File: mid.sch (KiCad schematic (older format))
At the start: 26 parts, among them P1 POLOLU_MICROSD1, P2 ADAFRUIT_MICROSD1, P3 EBAY_MICROSD1, P4 POLOLU_MICROSD2, P5 ADAFRUIT_MICROSD2, P6 EBAY_MICROSD2, P7 SPI, P8 RC2014_STANDARD_DEV_39, SW1 SW_DIP_x04, U1 TP3465-PLCC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

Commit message: add PCB
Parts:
- removed P7: SPI, symbol CONN_01X08
- added P7: SPI, Connector_PinHeader_2.54mm:PinHeader_1x09_P2.54mm_Vertical, symbol CONN_01X09
- C1, C2, C3: footprint (none) -> Capacitor_THT:C_Rect_L4.6mm_W2.0mm_P2.50mm_MKS02_FKP02
- C4: footprint (none) -> Capacitor_THT:CP_Radial_D5.0mm_P2.00mm
- JP1: footprint (none) -> Connector_PinHeader_2.54mm:PinHeader_1x02_P2.54mm_Vertical
- JP2, JP3: footprint (none) -> Connector_PinHeader_2.54mm:PinHeader_1x03_P2.54mm_Vertical
- P1, P4: footprint (none) -> Connector_PinHeader_2.54mm:PinHeader_1x09_P2.54mm_Vertical
- P2, P5: footprint (none) -> Connector_PinHeader_2.54mm:PinHeader_1x08_P2.54mm_Vertical
- P3, P6: footprint (none) -> Connector_PinHeader_2.54mm:PinHeader_1x06_P2.54mm_Vertical
- P8: footprint (none) -> Connector_PinHeader_2.54mm:PinHeader_1x39_P2.54mm_Vertical
- R1, R2, R3, R4, R5, R6, R7, R8: footprint (none) -> Resistor_THT:R_Axial_DIN0207_L6.3mm_D2.5mm_P7.62mm_Horizontal
- SW1: footprint (none) -> Button_Switch_THT:SW_DIP_SPSTx04_Piano_CTS_Series194-4MSTN_W7.62mm_P2.54mm
- U1: footprint (none) -> Package_LCC:PLCC-28_THT-Socket
- U2: footprint (none) -> Package_DIP:DIP-20_W7.62mm_Socket
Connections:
- net GND: now also P7.1 (P1)
- net MISO: now also P7.7 (P7)
- net MOSI: now also P7.8 (P8)
- net SCLK: now also P7.9 (P9)
- net VCC: now also P7.2 (P2)
- net ~SDCD1: now also P7.4 (P4)
- net ~SDCD2: now also P7.3 (P3)
- net ~SDCS1: now also P7.6 (P6)
- net ~SDCS2: now also P7.5 (P5)
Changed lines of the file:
@@
 LIBS:Switch
 LIBS:my_components
+LIBS:mid-cache
 EELAYER 25 0
 EELAYER END
@@
 Sheet 1 1
 Title "RC2014 MID"
-Date "2020-04-04"
+Date "2020-04-06"
 Rev ""
 Comp ""
@@
 F 0 "P8" H 2250 5950 50  0000 C CNN
 F 1 "RC2014_STANDARD_DEV_39" V 2000 3950 50  0000 C CNN
-F 2 "" H 2250 3950 50  0000 C CNN
+F 2 "Connector_PinHeader_2.54mm:PinHeader_1x39_P2.54mm_Vertical" H 2250 3950 50  0001 C CNN
 F 3 "" H 2250 3950 50  0000 C CNN
 	1    2250 3950
@@
 F 0 "U2" H 3550 4000 60  0000 L CNN
 F 1 "74HCT688" H 3550 2700 60  0000 L CNN
-F 2 "" H 3850 3350 60  0001 C CNN
+F 2 "Package_DIP:DIP-20_W7.62mm_Socket" H 3850 3350 60  0001 C CNN
 F 3 "" H 3850 3350 60  0001 C CNN
 	1    3850 3350
@@
 F 0 "SW1" H 5200 3900 50  0000 C CNN
 F 1 "SW_DIP_x04" H 5200 3300 50  0000 C CNN
-F 2 "" H 5200 3550 50  0001 C CNN
+F 2 "Button_Switch_THT:SW_DIP_SPSTx04_Piano_CTS_Series194-4MSTN_W7.62mm_P2.54mm" H 5200 3550 50  0001 C CNN
 F 3 "" H 5200 3550 50  0001 C CNN
 	1    5200 3550
@@
 F 0 "P2" H 7450 4450 50  0000 C CNN
 F 1 "ADAFRUIT_MICROSD1" V 7550 4000 50  0000 C CNN
-F 2 "" H 7450 4000 50  0000 C CNN
+F 2 "Connector_PinHeader_2.54mm:PinHeader_1x08_P2.54mm_Vertical" H 7450 4000 50  0001 C CNN
 F 3 "" H 7450 4000 50  0000 C CNN
 	1    7450 4000
@@
 F 0 "U1" H 4850 6700 60  0000 L CNN
 F 1 "TP3465-PLCC" H 4850 4500 60  0000 L CNN
-F 2 "" H 5150 5250 60  0001 C CNN
+F 2 "Package_LCC:PLCC-28_THT-Socket" H 5150 5250 60  0001 C CNN
 F 3 "" H 5150 5250 60  0001 C CNN
 	1    5150 5600
@@
 F 0 "R2" V 5050 2700 50  0000 L CNN
 F 1 "10K" V 5000 2600 50  0000 C CNN
-F 2 "" V 4930 2600 50  0000 C CNN
+F 2 "Resistor_THT:R_Axial_DIN0207_L6.3mm_D2.5mm_P7.62mm_Horizontal" V 4930 2600 50  0001 C CNN
 F 3 "" H 5000 2600 50  0000 C CNN
 	1    5000 2600
@@
 F 0 "R1" V 4950 2700 50  0000 L CNN
 F 1 "10K" V 4900 2600 50  0000 C CNN
-F 2 "" V 4830 2600 50  0000 C CNN
+F 2 "Resistor_THT:R_Axial_DIN0207_L6.3mm_D2.5mm_P7.62mm_Horizontal" V 4830 2600 50  0001 C CNN
 F 3 "" H 4900 2600 50  0000 C CNN
 	1    4900 2600
@@
 F 0 "R3" V 5150 2700 50  0000 L CNN
 F 1 "10K" V 5100 2600 50  0000 C CNN
-F 2 "" V 5030 2600 50  0000 C CNN
+F 2 "Resistor_THT:R_Axial_DIN0207_L6.3mm_D2.5mm_P7.62mm_Horizontal" V 5030 2600 50  0001 C CNN
 F 3 "" H 5100 2600 50  0000 C CNN
 	1    5100 2600
@@
 F 0 "R4" V 5250 2700 50  0000 L CNN
 F 1 "10K" V 5200 2600 50  0000 C CNN
-F 2 "" V 5130 2600 50  0000 C CNN
+F 2 "Resistor_THT:R_Axial_DIN0207_L6.3mm_D2.5mm_P7.62mm_Horizontal" V 5130 2600 50  0001 C CNN
 F 3 "" H 5200 2600 50  0000 C CNN
 	1    5200 2600
@@
 F 0 "R5" V 5350 2700 50  0000 L CNN
 F 1 "10K" V 5300 2600 50  0000 C CNN
-F 2 "" V 5230 2600 50  0000 C CNN
+F 2 "Resistor_THT:R_Axial_DIN0207_L6.3mm_D2.5mm_P7.62mm_Horizontal" V 5230 2600 50  0001 C CNN
 F 3 "" H 5300 2600 50  0000 C CNN
 	1    5300 2600
@@
 F 0 "R7" V 6550 1900 50  0000 C CNN
 F 1 "10K" V 6450 1900 50  0000 C CNN
-F 2 "" V 6380 1900 50  0000 C CNN
+F 2 "Resistor_THT:R_Axial_DIN0207_L6.3mm_D2.5mm_P7.62mm_Horizontal" V 6380 1900 50  0001 C CNN
 F 3 "" H 6450 1900 50  0000 C CNN
 	1    6450 1900
@@
 F 0 "JP2" H 6500 1450 50  0000 L CNN
 F 1 "SDCD1_PULL" H 6450 1650 50  0000 C BNN
-F 2 "" H 6450 1550 50  0000 C CNN
+F 2 "Connector_PinHeader_2.54mm:PinHeader_1x03_P2.54mm_Vertical" H 6450 1550 50  0001 C CNN
 F 3 "" H 6450 1550 50  0000 C CNN
 	1    6450 1550
@@
 F 0 "P3" H 7450 6050 50  0000 C CNN
 F 1 "EBAY_MICROSD1" V 7550 5700 50  0000 C CNN
-F 2 "" H 7450 5700 50  0000 C CNN
+F 2 "Connector_PinHeader_2.54mm:PinHeader_1x06_P2.54mm_Vertical" H 7450 5700 50  0001 C CNN
 F 3 "" H 7450 5700 50  0000 C CNN
 	1    7450 5700
@@
 F 0 "P4" H 9050 3450 50  0000 C CNN
 F 1 "POLOLU_MICROSD2" V 9150 2950 50  0000 C CNN
-F 2 "" H 9050 2950 50  0000 C CNN
+F 2 "Connector_PinHeader_2.54mm:PinHeader_1x09_P2.54mm_Vertical" H 9050 2950 50  0001 C CNN
 F 3 "" H 9050 2950 50  0000 C CNN
 	1    9050 2950
@@
 F 0 "P1" H 7450 3450 50  0000 C CNN
 F 1 "POLOLU_MICROSD1" V 7550 2950 50  0000 C CNN
-F 2 "" H 7450 2950 50  0000 C CNN
+F 2 "Connector_PinHeader_2.54mm:PinHeader_1x09_P2.54mm_Vertical" H 7450 2950 50  0001 C CNN
 F 3 "" H 7450 2950 50  0000 C CNN
 	1    7450 2950
@@
 F 0 "P5" H 9050 4450 50  0000 C CNN
 F 1 "ADAFRUIT_MICROSD2" V 9150 4000 50  0000 C CNN
-F 2 "" H 9050 4000 50  0000 C CNN
+F 2 "Connector_PinHeader_2.54mm:PinHeader_1x08_P2.54mm_Vertical" H 9050 4000 50  0001 C CNN
 F 3 "" H 9050 4000 50  0000 C CNN
 	1    9050 4000
@@
 F 0 "P6" H 9050 6050 50  0000 C CNN
 F 1 "EBAY_MICROSD2" V 9150 5700 50  0000 C CNN
-F 2 "" H 9050 5700 50  0000 C CNN
+F 2 "Connector_PinHeader_2.54mm:PinHeader_1x06_P2.54mm_Vertical" H 9050 5700 50  0001 C CNN
 F 3 "" H 9050 5700 50  0000 C CNN
 	1    9050 5700
@@
 F 0 "JP1" H 6100 2430 50  0000 C CNN
 F 1 "MISO_PULLUP" H 6110 2290 50  0000 C CNN
-F 2 "" H 6100 2350 50  0000 C CNN
+F 2 "Connector_PinHeader_2.54mm:PinHeader_1x02_P2.54mm_Vertical" H 6100 2350 50  0001 C CNN
 F 3 "" H 6100 2350 50  0000 C CNN
 	1    6100 2350
@@
 F 0 "R6" V 6200 1900 50  0000 C CNN
 F 1 "10K" V 6100 1900 50  0000 C CNN
-F 2 "" V 6030 1900 50  0000 C CNN
+F 2 "Resistor_THT:R_Axial_DIN0207_L6.3mm_D2.5mm_P7.62mm_Horizontal" V 6030 1900 50  0001 C CNN
 F 3 "" H 6100 1900 50  0000 C CNN
 	1    6100 1900
@@
 F 0 "R8" V 8150 1950 50  0000 C CNN
 F 1 "10K" V 8050 1950 50  0000 C CNN
-F 2 "" V 7980 1950 50  0000 C CNN
+F 2 "Resistor_THT:R_Axial_DIN0207_L6.3mm_D2.5mm_P7.62mm_Horizontal" V 7980 1950 50  0001 C CNN
 F 3 "" H 8050 1950 50  0000 C CNN
 	1    8050 1950
@@
 F 0 "JP3" H 8100 1450 50  0000 L CNN
 F 1 "SDCD2_PULL" H 8050 1650 50  0000 C BNN
-F 2 "" H 8050 1550 50  0000 C CNN
+F 2 "Connector_PinHeader_2.54mm:PinHeader_1x03_P2.54mm_Vertical" H 8050 1550 50  0001 C CNN
 F 3 "" H 8050 1550 50  0000 C CNN
 	1    8050 1550
@@
 F 0 "C4" H 3310 7520 50  0000 L CNN
 F 1 "10µF" H 3310 7370 50  0000 L CNN
-F 2 "" H 3300 7450 50  0000 C CNN
+F 2 "Capacitor_THT:CP_Radial_D5.0mm_P2.00mm" H 3300 7450 50  0001 C CNN
 F 3 "" H 3300 7450 50  0000 C CNN
 	1    3300 7450
@@
 F 0 "C2" H 2510 7520 50  0000 L CNN
 F 1 "100nF" H 2510 7370 50  0000 L CNN
-F 2 "" H 2500 7450 50  0000 C CNN
+F 2 "Capacitor_THT:C_Rect_L4.6mm_W2.0mm_P2.50mm_MKS02_FKP02" H 2500 7450 50  0001 C CNN
 F 3 "" H 2500 7450 50  0000 C CNN
 	1    2500 7450
@@
 F 0 "C3" H 2910 7520 50  0000 L CNN
 F 1 "100nF" H 2910 7370 50  0000 L CNN
-F 2 "" H 2900 7450 50  0000 C CNN
+F 2 "Capacitor_THT:C_Rect_L4.6mm_W2.0mm_P2.50mm_MKS02_FKP02" H 2900 7450 50  0001 C CNN
 F 3 "" H 2900 7450 50  0000 C CNN
 	1    2900 7450
@@
 F 0 "C1" H 2110 7520 50  0000 L CNN
 F 1 "100nF" H 2110 7370 50  0000 L CNN
-F 2 "" H 2100 7450 50  0000 C CNN
+F 2 "Capacitor_THT:C_Rect_L4.6mm_W2.0mm_P2.50mm_MKS02_FKP02" H 2100 7450 50  0001 C CNN
 F 3 "" H 2100 7450 50  0000 C CNN
 	1    2100 7450
@@
 	3300 7550 3300 7600
 Connection ~ 3300 7600
-$Comp
-L CONN_01X08 P7
-U 1 1 5E8A7DE2
-P 10250 5000
-F 0 "P7" H 10250 5450 50  0000 C CNN
-F 1 "SPI" V 10350 5000 50  0000 C CNN
-F 2 "" H 10250 5000 50  0000 C CNN
-F 3 "" H 10250 5000 50  0000 C CNN
-	1    10250 5000
-	1    0    0    1
-$EndComp
 Connection ~ 6450 5150
 Connection ~ 8050 5250
@@
 L GND #PWR014
 U 1 1 5E8A8639
-P 9450 6050
-F 0 "#PWR014" H 9450 5800 50  0001 C CNN
-F 1 "GND" H 9450 5900 50  0000 C CNN
-F 2 "" H 9450 6050 50  0000 C CNN
-F 3 "" H 9450 6050 50  0000 C CNN
-	1    9450 6050
-	1    0    0    -1
-$EndComp
-Wire Wire Line
-	10050 5350 9450 5350
-Wire Wire Line
-	9450 5350 9450 6050
+P 9950 5550
+F 0 "#PWR014" H 9950 5300 50  0001 C CNN
+F 1 "GND" H 9950 5400 50  0000 C CNN
+F 2 "" H 9950 5550 50  0000 C CNN
+F 3 "" H 9950 5550 50  0000 C CNN
+	1    9950 5550
+	1    0    0    -1
+$EndComp
+$Comp
+L CONN_01X09 P7
+U 1 1 5E8BE610
+P 10250 5050
+F 0 "P7" H 10250 5550 50  0000 C CNN
+F 1 "SPI" V 10350 5050 50  0000 C CNN
+F 2 "Connector_PinHeader_2.54mm:PinHeader_1x09_P2.54mm_Vertical" H 10250 5050 50  0001 C CNN
+F 3 "" H 10250 5050 50  0000 C CNN
+	1    10250 5050
+	1    0    0    1
+$EndComp
+$Comp
+L VCC #PWR015
+U 1 1 5E8BE8AD
+P 9950 4550
+F 0 "#PWR015" H 9950 4400 50  0001 C CNN
+F 1 "VCC" H 9950 4700 50  0000 C CNN
+F 2 "" H 9950 4550 50  0000 C CNN
+F 3 "" H 9950 4550 50  0000 C CNN
+	1    9950 4550
+	1    0    0    -1
+$EndComp
+Wire Wire Line
+	10050 5450 9950 5450
+Wire Wire Line
+	9950 5450 9950 5550
+Wire Wire Line
+	10050 5350 9950 5350
+Wire Wire Line
+	9950 5350 9950 4550
 $EndSCHEMATC

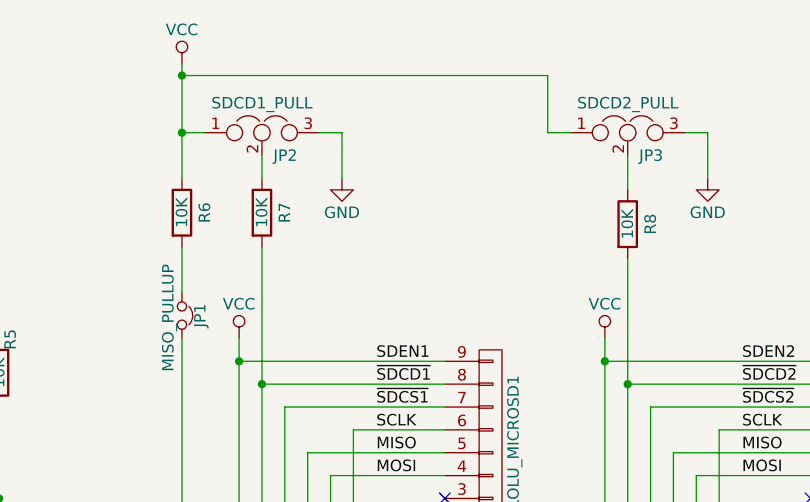
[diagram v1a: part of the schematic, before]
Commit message: switch pull-ups to 100K
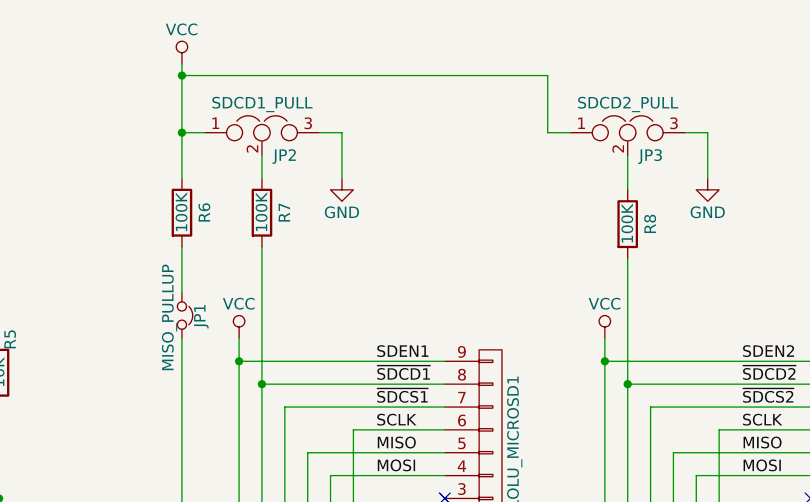
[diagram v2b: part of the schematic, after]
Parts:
- R6, R7, R8: value 10K -> 100K
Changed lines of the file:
@@
 Sheet 1 1
 Title "RC2014 MID"
-Date "2020-04-06"
+Date "2020-04-20"
 Rev ""
 Comp ""
@@
 P 6450 1900
 F 0 "R7" V 6550 1900 50  0000 C CNN
-F 1 "10K" V 6450 1900 50  0000 C CNN
+F 1 "100K" V 6450 1900 50  0000 C CNN
 F 2 "Resistor_THT:R_Axial_DIN0207_L6.3mm_D2.5mm_P7.62mm_Horizontal" V 6380 1900 50  0001 C CNN
 F 3 "" H 6450 1900 50  0000 C CNN
@@
 P 6100 1900
 F 0 "R6" V 6200 1900 50  0000 C CNN
-F 1 "10K" V 6100 1900 50  0000 C CNN
+F 1 "100K" V 6100 1900 50  0000 C CNN
 F 2 "Resistor_THT:R_Axial_DIN0207_L6.3mm_D2.5mm_P7.62mm_Horizontal" V 6030 1900 50  0001 C CNN
 F 3 "" H 6100 1900 50  0000 C CNN
@@
 P 8050 1950
 F 0 "R8" V 8150 1950 50  0000 C CNN
-F 1 "10K" V 8050 1950 50  0000 C CNN
+F 1 "100K" V 8050 1950 50  0000 C CNN
 F 2 "Resistor_THT:R_Axial_DIN0207_L6.3mm_D2.5mm_P7.62mm_Horizontal" V 7980 1950 50  0001 C CNN
 F 3 "" H 8050 1950 50  0000 C CNN
